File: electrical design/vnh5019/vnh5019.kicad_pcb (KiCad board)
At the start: 2 copper layers, 71 x 30 mm, 20 parts, among them J1 XT30UPBF, J2 Conn_01x06_Male, J3 Conn_01x01_Female, J4 Conn_01x01_Female, Q1 Q_NMOS_GDS, U1 VNH5019A-E

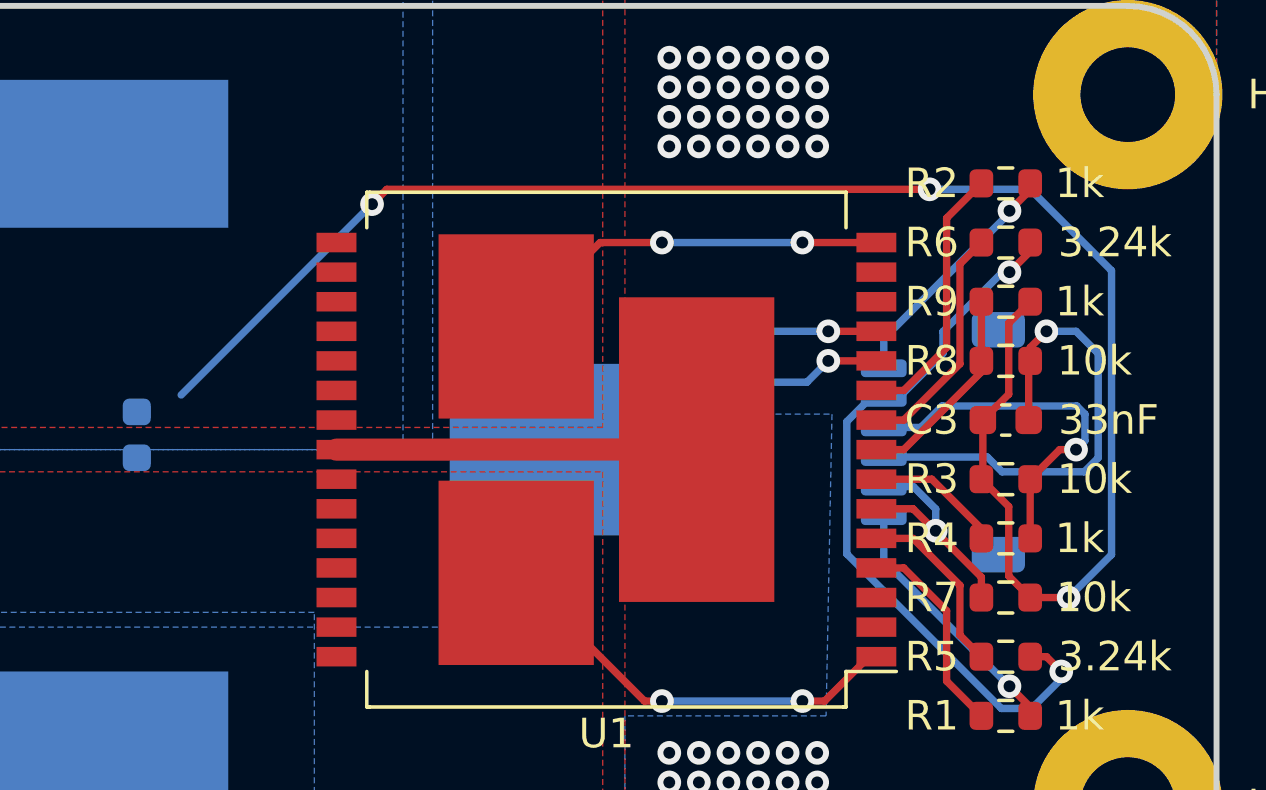
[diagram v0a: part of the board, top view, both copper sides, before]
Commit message: change driver output connector to 5 pins
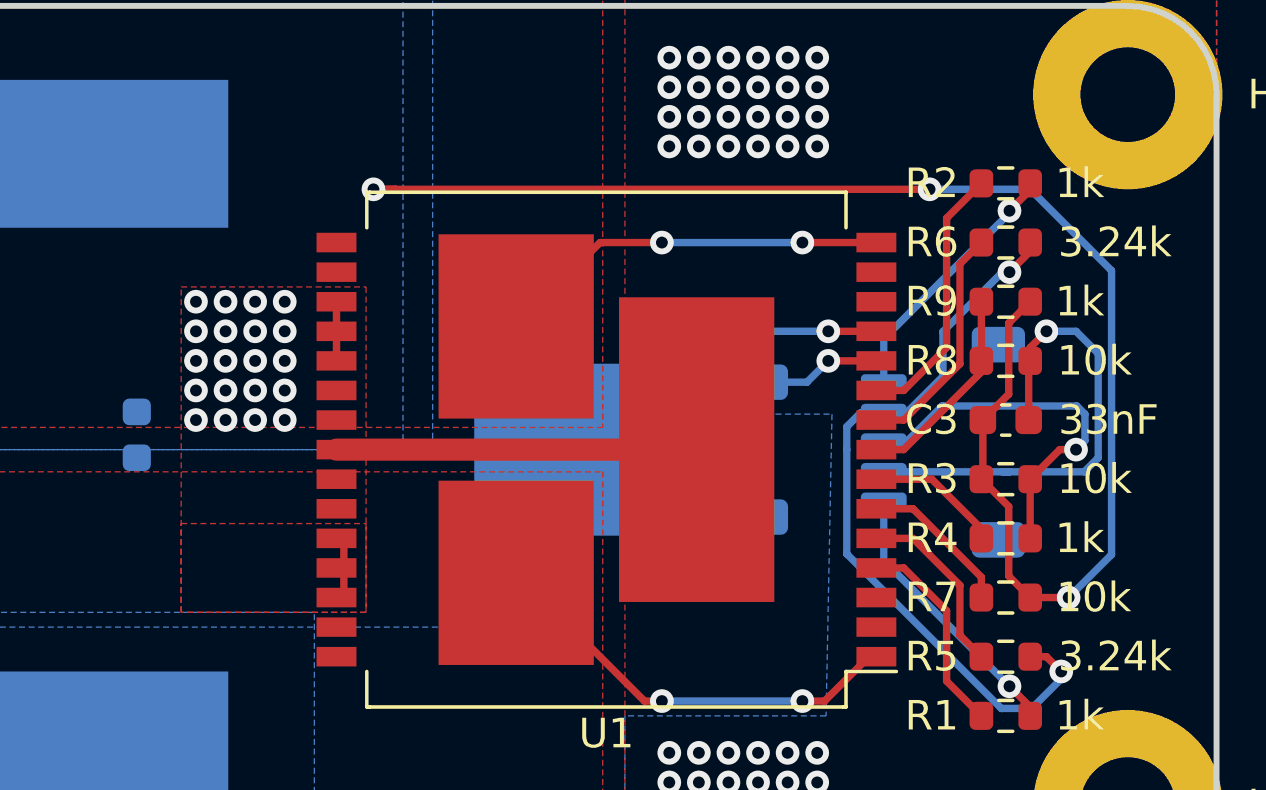
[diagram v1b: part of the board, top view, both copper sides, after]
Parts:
- J2: value Conn_01x06_Male -> SH1.0 5P; footprint Connector_JST:JST_SH_SM06B-SRSS-TB_1x06-1MP_P1.00mm_Horizontal -> Connector_JST:JST_SH_SM05B-SRSS-TB_1x05-1MP_P1.00mm_Horizontal
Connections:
- net +3V3 renamed /EN
- J2 pad 5: /CS_DIS -> /INA
- R7 pad 2: /CS_DIS -> Net-(U1-CS_DIS)
- U1 pad 6: /CS_DIS -> Net-(U1-CS_DIS)
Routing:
- net /CS_DIS: track 8.00 -> 0.00 mm, vias 1 -> 0
- net Net-(U1-CS_DIS): track 0.00 -> 5.20 mm
- net GND: track 59.8 -> 54.7 mm, vias 3 -> 23
- net /INB: track 8.30 -> 8.80 mm
- net /INA: track 8.80 -> 9.30 mm
- added copper zone on F.Cu, net GND
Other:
- board text added: "+12V"
- board text removed: "12V"

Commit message: update pcbs and mech drawings
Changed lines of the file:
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@@
     (polygon
       (pts
-        (xy 116.8 114)
+        (xy 117 114)
         (xy 110 114)
         (xy 110 120.6)

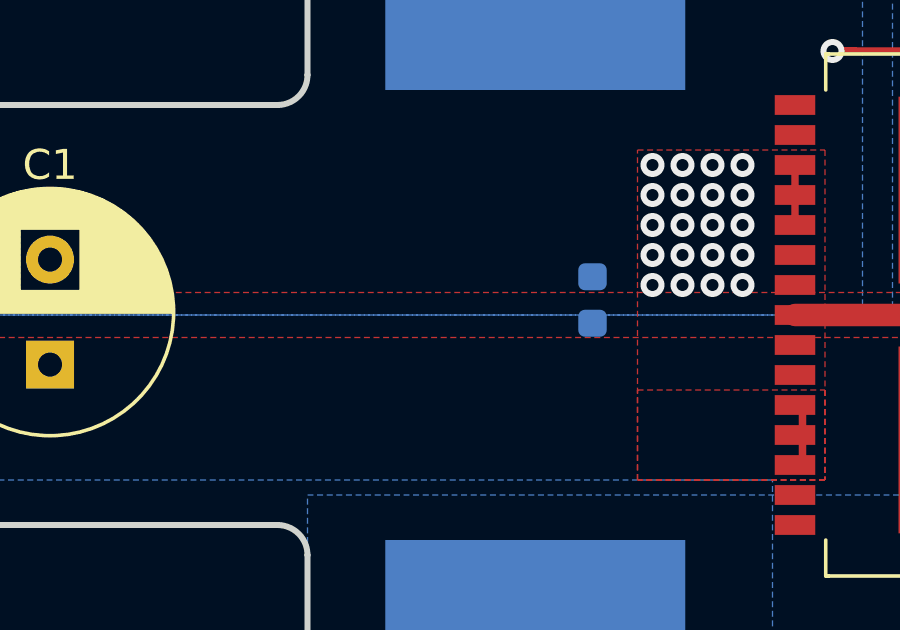
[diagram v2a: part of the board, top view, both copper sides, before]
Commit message: add indicator leds to driver pcb
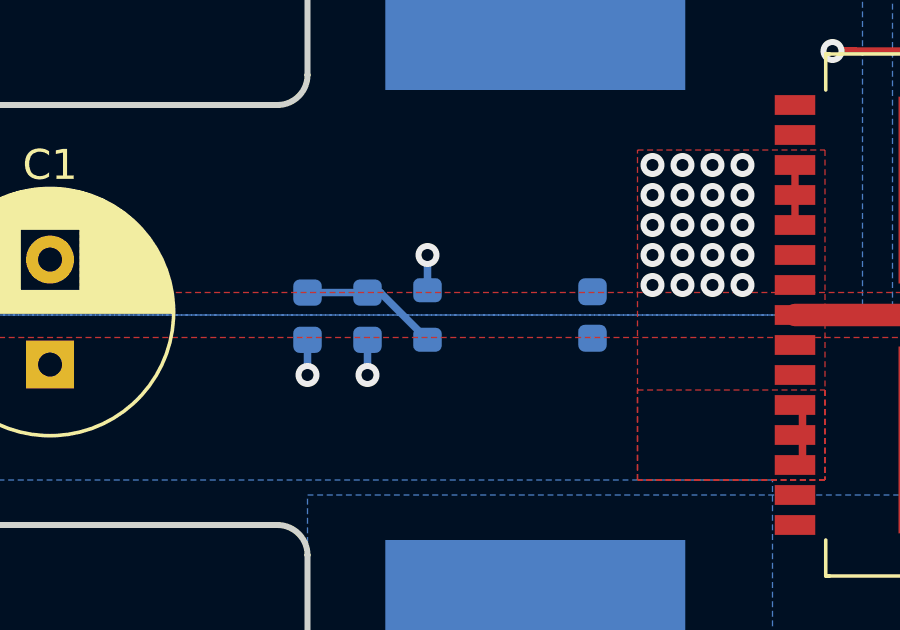
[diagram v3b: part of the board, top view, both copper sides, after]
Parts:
- added D1: G, Diode_SMD:D_0603_1608Metric, B.Cu at (84.0, 105.0)
- added D2: R, Diode_SMD:D_0603_1608Metric, B.Cu at (86.0, 105.0)
- added R10: 4.7k, Resistor_SMD:R_0603_1608Metric, B.Cu at (88.0, 105.0)
- moved C2 0.50 mm to (93.5, 105.0)
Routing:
- net Net-(D1-K): track 0.00 -> 4.65 mm
- net /OUTA: track 14.6 -> 16.9 mm, vias 2 -> 4
- net /OUTB: track 13.3 -> 14.5 mm, vias 2 -> 3

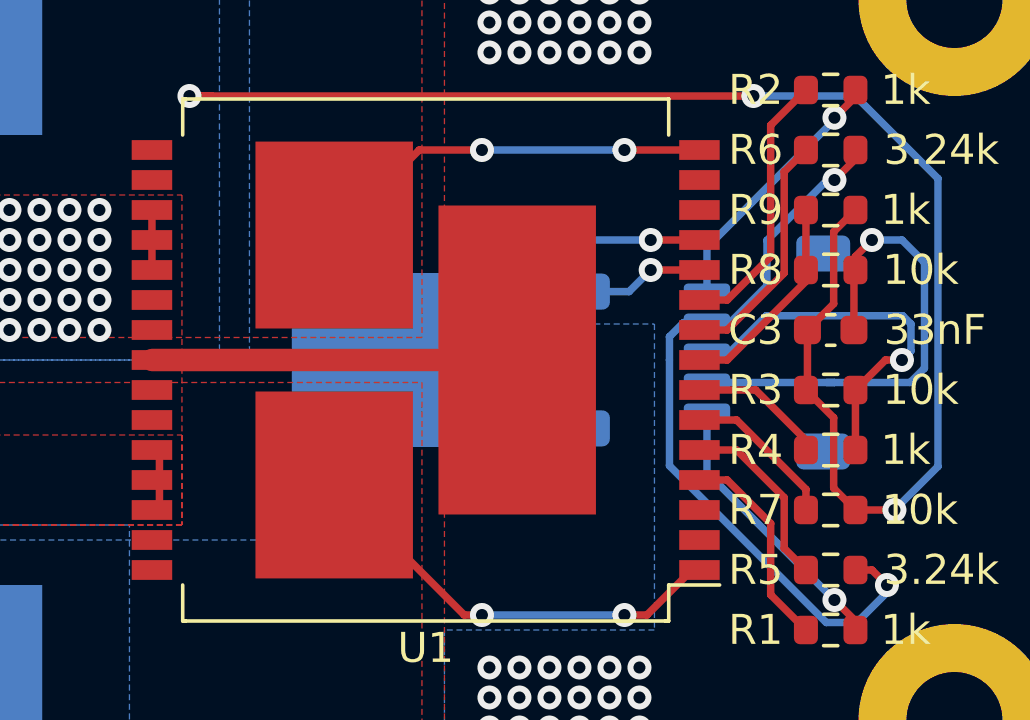
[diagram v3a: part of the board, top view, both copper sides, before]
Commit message: add jlc order number silkscreen
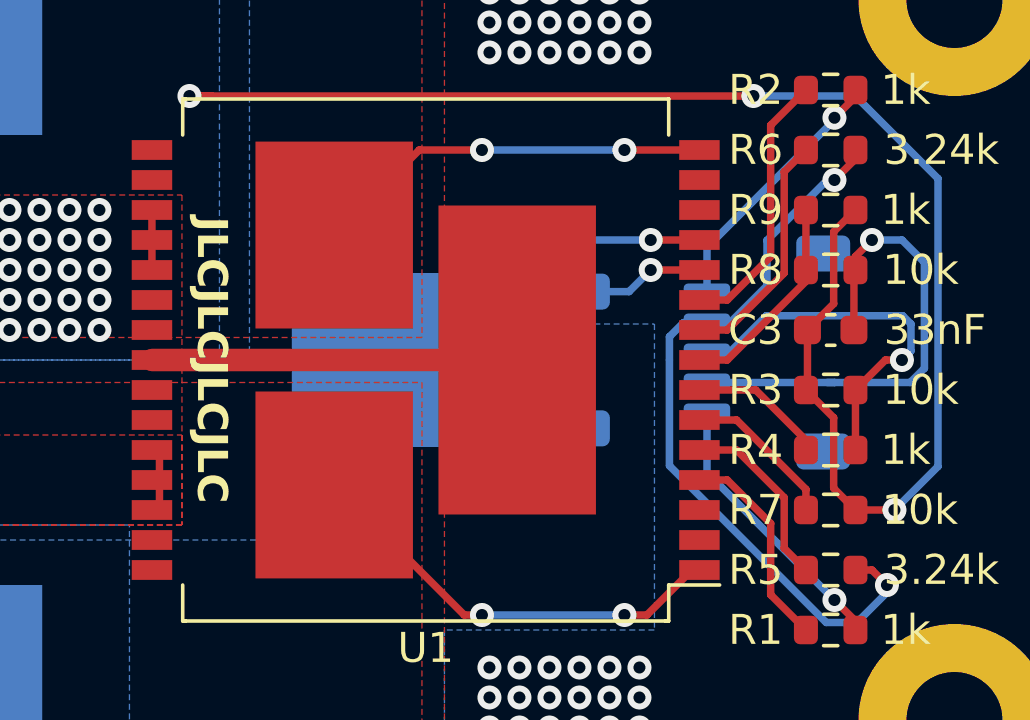
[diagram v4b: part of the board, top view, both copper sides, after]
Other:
- board text added: "JLCJLCJLCJLC"
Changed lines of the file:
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@@
       (plot_on_all_layers_selection 0x0000000_00000000)
       (disableapertmacros false)
-      (usegerberextensions false)
-      (usegerberattributes true)
-      (usegerberadvancedattributes true)
-      (creategerberjobfile true)
+      (usegerberextensions true)
+      (usegerberattributes false)
+      (usegerberadvancedattributes false)
+      (creategerberjobfile false)
       (dashed_line_dash_ratio 12.000000)
       (dashed_line_gap_ratio 3.000000)
@@
       (plotinvisibletext false)
       (sketchpadsonfab false)
-      (subtractmaskfromsilk false)
+      (subtractmaskfromsilk true)
       (outputformat 1)
       (mirror false)
-      (drillshape 1)
+      (drillshape 0)
       (scaleselection 1)
-      (outputdirectory "")
+      (outputdirectory "fabrication")
     )
   )
@@
     (fp_line (start 4.11 2.7) (end 4.11 -2.7)
       (stroke (width 0.1) (type solid)) (layer "B.Fab"))
-    (pad "1" smd roundrect (at -5.04 2.28 180) (size 2.2 1.2) (layers "B.Cu" "B.Paste" "B.Mask") (roundrect_rratio 0.208333)
+    (pad "1" smd roundrect (at -5.04 2.28 180) (size 2.2 1.2) (layers "B.Cu" "B.Paste" "B.Mask") (roundrect_rratio 0.2083333333)
       (net 17 "/CP") (pinfunction "G") (pintype "input"))
-    (pad "2" smd roundrect (at -0.415 -1.525 180) (size 3.05 2.75) (layers "B.Cu" "B.Paste") (roundrect_rratio 0.090909)
+    (pad "2" smd roundrect (at -0.415 -1.525 180) (size 3.05 2.75) (layers "B.Cu" "B.Paste") (roundrect_rratio 0.09090909091)
       (net 1 "Net-(Q1-D)") (pinfunction "D") (pintype "passive"))
-    (pad "2" smd roundrect (at -0.415 1.525 180) (size 3.05 2.75) (layers "B.Cu" "B.Paste") (roundrect_rratio 0.090909)
+    (pad "2" smd roundrect (at -0.415 1.525 180) (size 3.05 2.75) (layers "B.Cu" "B.Paste") (roundrect_rratio 0.09090909091)
       (net 1 "Net-(Q1-D)") (pinfunction "D") (pintype "passive"))
-    (pad "2" smd roundrect (at 1.26 0 180) (size 6.4 5.8) (layers "B.Cu" "B.Mask") (roundrect_rratio 0.043103)
+    (pad "2" smd roundrect (at 1.26 0 180) (size 6.4 5.8) (layers "B.Cu" "B.Mask") (roundrect_rratio 0.04310293103)
       (net 1 "Net-(Q1-D)") (pinfunction "D") (pintype "passive"))
-    (pad "2" smd roundrect (at 2.935 -1.525 180) (size 3.05 2.75) (layers "B.Cu" "B.Paste") (roundrect_rratio 0.090909)
+    (pad "2" smd roundrect (at 2.935 -1.525 180) (size 3.05 2.75) (layers "B.Cu" "B.Paste") (roundrect_rratio 0.09090909091)
       (net 1 "Net-(Q1-D)") (pinfunction "D") (pintype "passive"))
-    (pad "2" smd roundrect (at 2.935 1.525 180) (size 3.05 2.75) (layers "B.Cu" "B.Paste") (roundrect_rratio 0.090909)
+    (pad "2" smd roundrect (at 2.935 1.525 180) (size 3.05 2.75) (layers "B.Cu" "B.Paste") (roundrect_rratio 0.09090909091)
       (net 1 "Net-(Q1-D)") (pinfunction "D") (pintype "passive"))
-    (pad "3" smd roundrect (at -5.04 -2.28 180) (size 2.2 1.2) (layers "B.Cu" "B.Paste" "B.Mask") (roundrect_rratio 0.208333)
+    (pad "3" smd roundrect (at -5.04 -2.28 180) (size 2.2 1.2) (layers "B.Cu" "B.Paste" "B.Mask") (roundrect_rratio 0.2083333333)
       (net 18 "+12V") (pinfunction "S") (pintype "passive"))
     (model "${KICAD6_3DMODEL_DIR}/Package_TO_SOT_SMD.3dshapes/TO-252-2.wrl"
@@
     (pad "5" smd roundrect (at 2 2 270) (size 0.6 1.55) (layers "B.Cu" "B.Paste" "B.Mask") (roundrect_rratio 0.25)
       (net 4 "/INA") (pinfunction "Pin_5") (pintype "passive"))
-    (pad "MP" smd roundrect (at -3.3 -1.875 270) (size 1.2 1.8) (layers "B.Cu" "B.Paste" "B.Mask") (roundrect_rratio 0.208333))
-    (pad "MP" smd roundrect (at 3.3 -1.875 270) (size 1.2 1.8) (layers "B.Cu" "B.Paste" "B.Mask") (roundrect_rratio 0.208333))
+    (pad "MP" smd roundrect (at -3.3 -1.875 270) (size 1.2 1.8) (layers "B.Cu" "B.Paste" "B.Mask") (roundrect_rratio 0.2083333333))
+    (pad "MP" smd roundrect (at 3.3 -1.875 270) (size 1.2 1.8) (layers "B.Cu" "B.Paste" "B.Mask") (roundrect_rratio 0.2083333333))
     (model "${KICAD6_3DMODEL_DIR}/Connector_JST.3dshapes/JST_SH_SM05B-SRSS-TB_1x05-1MP_P1.00mm_Horizontal.step"
       (offset (xyz 0 1 0))
@@
         (effects (font (size 1 1) (thickness 0.15)) (justify mirror))
     )
-    (fp_text value "1µf" (at 0 -1.43 90) (layer "B.SilkS")
+    (fp_text value "1µf" (at 0 -1.75 90) (layer "B.SilkS")
         (effects (font (size 1 1) (thickness 0.15)) (justify mirror))
     )
@@
     (effects (font (size 1.5 1.5) (thickness 0.3)) (justify mirror))
   )
+  (gr_text "JLCJLCJLCJLC" (at 102.25 105 270) (layer "F.SilkS")
+    (effects (font (size 1 1) (thickness 0.2) bold))
+  )
   (segment (start 112.425 105) (end 100.25 105) (width 0.75) (layer "F.Cu") (net 1))

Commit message: finalise pcbs for production
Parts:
- added G***: LOGO, LOGO, F.Cu at (89.4, 103.9)
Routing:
- net /OUTB: track 14.5 -> 15.8 mm
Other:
- board text added: "ducc."
